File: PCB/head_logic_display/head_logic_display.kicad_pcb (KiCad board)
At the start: 2 copper layers, 48 x 21.6 mm, 71 parts, among them J1 Conn_01x03_Socket, J2 Conn_01x03_Socket

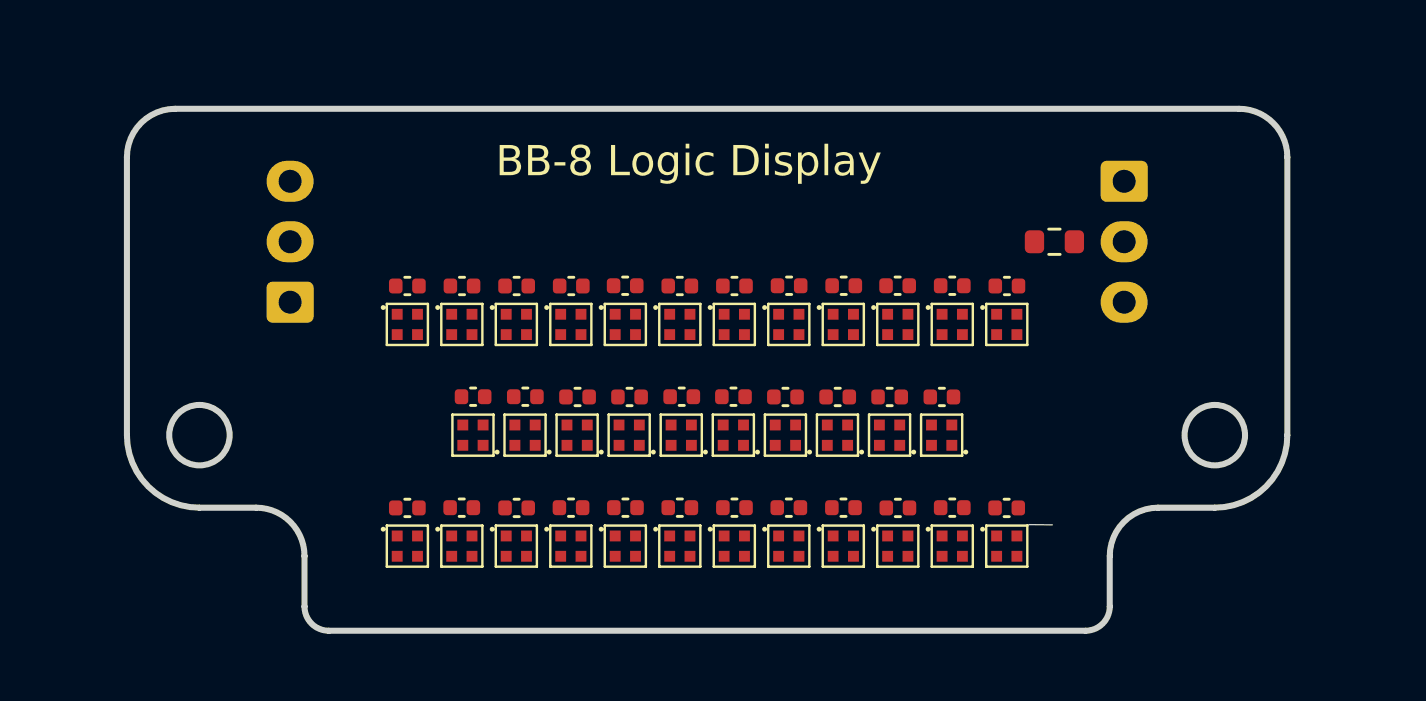
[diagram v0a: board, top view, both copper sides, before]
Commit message: Finish component placement
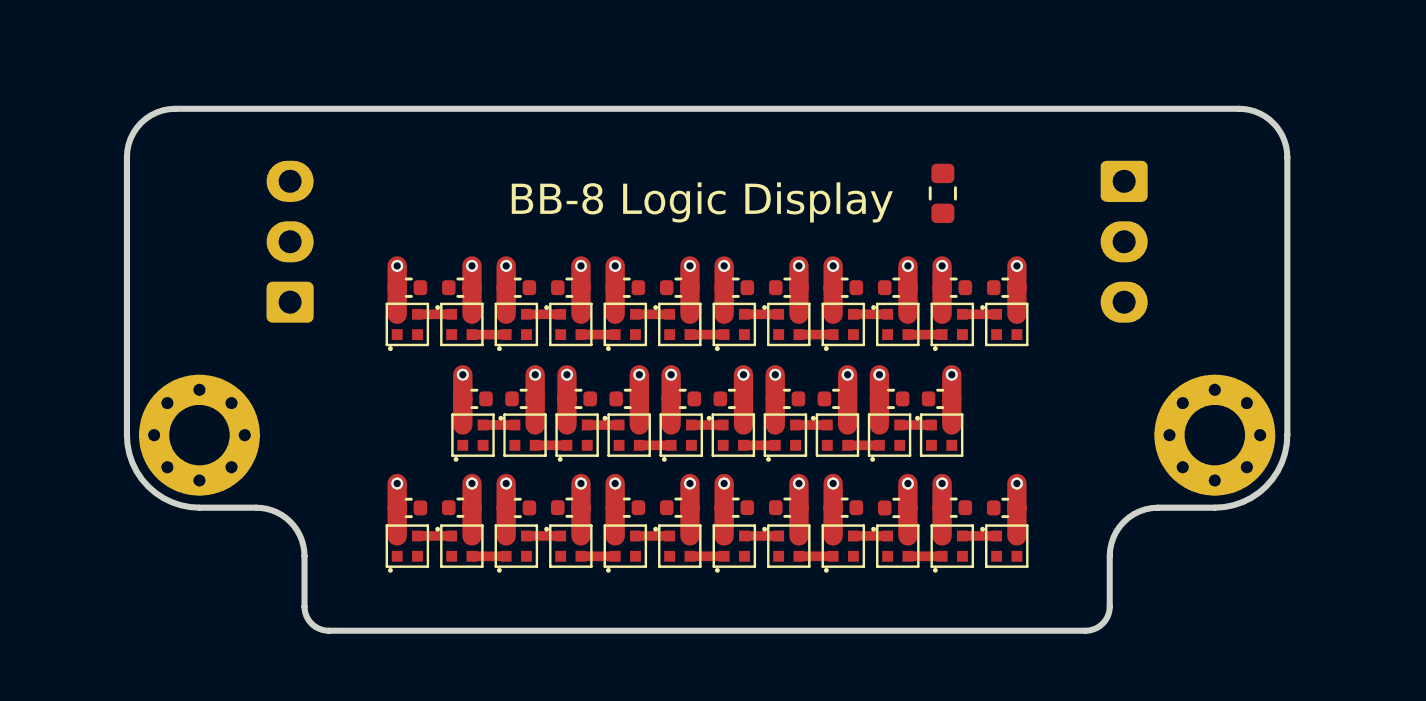
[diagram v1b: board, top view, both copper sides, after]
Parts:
- added REF**: MountingHole_2.5mm_Pad_Via, MountingHole:MountingHole_2.5mm_Pad_Via, F.Cu at (70.2, 97.0)
- added REF**: MountingHole_2.5mm_Pad_Via, MountingHole:MountingHole_2.5mm_Pad_Via, F.Cu at (112.2, 97.0)
- moved LED22 19.4 mm to (101.0, 97.0), turned to 0 degrees
- moved LED27 19.4 mm to (81.6, 97.0), turned to 90 degrees
- moved C22 19.3 mm to (81.6, 95.5), turned to 0 degrees
- moved C13 19.3 mm to (100.9, 95.5)
- moved C21 15.1 mm to (83.7, 95.5)
- moved C14 15.1 mm to (98.9, 95.5), turned to 0 degrees
- moved LED23 15.1 mm to (83.7, 97.0), turned to 0 degrees
- moved LED26 15.1 mm to (98.8, 97.0), turned to 90 degrees
- moved LED18 10.8 mm to (85.9, 97.0), turned to 90 degrees
- moved LED30 10.8 mm to (96.6, 97.0), turned to 0 degrees
- moved C20 10.7 mm to (85.9, 95.5), turned to 0 degrees
- moved C15 10.7 mm to (96.6, 95.5)
- moved C19 6.52 mm to (88.0, 95.5)
- moved C16 6.51 mm to (94.5, 95.5), turned to 0 degrees
- moved LED13 6.46 mm to (88.0, 97.0), turned to 0 degrees
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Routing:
- net +5V: track 0.00 -> 70.8 mm, vias 0 -> 34
- net Net-(LED36-DOUT): track 0.00 -> 1.41 mm
- net Net-(LED35-DOUT): track 0.00 -> 1.41 mm
- net Net-(LED31-DOUT): track 0.00 -> 1.41 mm
- net Net-(LED29-DOUT): track 0.00 -> 1.41 mm
- net Net-(LED28-DOUT): track 0.00 -> 1.41 mm
- net Net-(LED24-DOUT): track 0.00 -> 1.41 mm
- net Net-(LED21-DOUT): track 0.00 -> 1.41 mm
- net Net-(LED2-DIN): track 0.00 -> 1.41 mm
- net Net-(LED16-DOUT): track 0.00 -> 1.41 mm
- net Net-(LED14-DOUT): track 0.00 -> 1.41 mm
- net Net-(LED14-DIN): track 0.00 -> 1.41 mm
- net Net-(LED12-DOUT): track 0.00 -> 1.41 mm
- net Net-(LED12-DIN): track 0.00 -> 1.41 mm
- net Net-(LED11-DIN): track 0.00 -> 1.41 mm
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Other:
- outline, holes or cut-outs redrawn

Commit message: Finish board layout
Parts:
- removed REF** (x2): MountingHole_2.5mm_Pad_Via, MountingHole:MountingHole_2.5mm_Pad_Via
- added H1: MountingHole_Pad, MountingHole:MountingHole_2.5mm_Pad_Via, F.Cu at (70.2, 97.0)
- added H2: MountingHole_Pad, MountingHole:MountingHole_2.5mm_Pad_Via, F.Cu at (112.2, 97.0)
- moved R1 6.31 mm to (106.2, 90.7)
- moved C24 0.20 mm to (101.5, 100.2)
- moved C26 0.20 mm to (96.9, 100.2)
- moved C27 0.20 mm to (94.6, 100.2)
- moved C28 0.20 mm to (92.4, 100.2)
- moved C29 0.20 mm to (90.1, 100.2)
- moved C30 0.20 mm to (87.9, 100.2)
- moved C31 0.20 mm to (85.6, 100.2)
- moved C33 0.20 mm to (81.0, 100.2)
- moved C23 0.19 mm to (103.6, 100.2)
- moved C25 0.19 mm to (99.1, 100.2)
- moved C32 0.19 mm to (83.4, 100.2)
- moved C34 0.19 mm to (78.9, 100.2)
- moved C1 0.15 mm to (103.6, 91.0)
- moved C10 0.15 mm to (83.4, 91.0)
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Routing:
- net Net-(LED17-DOUT): track 0.00 -> 36.6 mm, vias 0 -> 2
- net Net-(LED27-DOUT): track 0.00 -> 35.4 mm, vias 0 -> 2
- net /DATA_OUT: track 0.00 -> 19.0 mm, vias 0 -> 1
- net Net-(LED1-DIN): track 0.00 -> 3.11 mm
- net /DATA_IN: track 0.00 -> 2.60 mm
- net +5V: track 70.8 -> 69.6 mm
- added copper zone on B.Cu, net +5V
- added copper zone on F.Cu, net GND

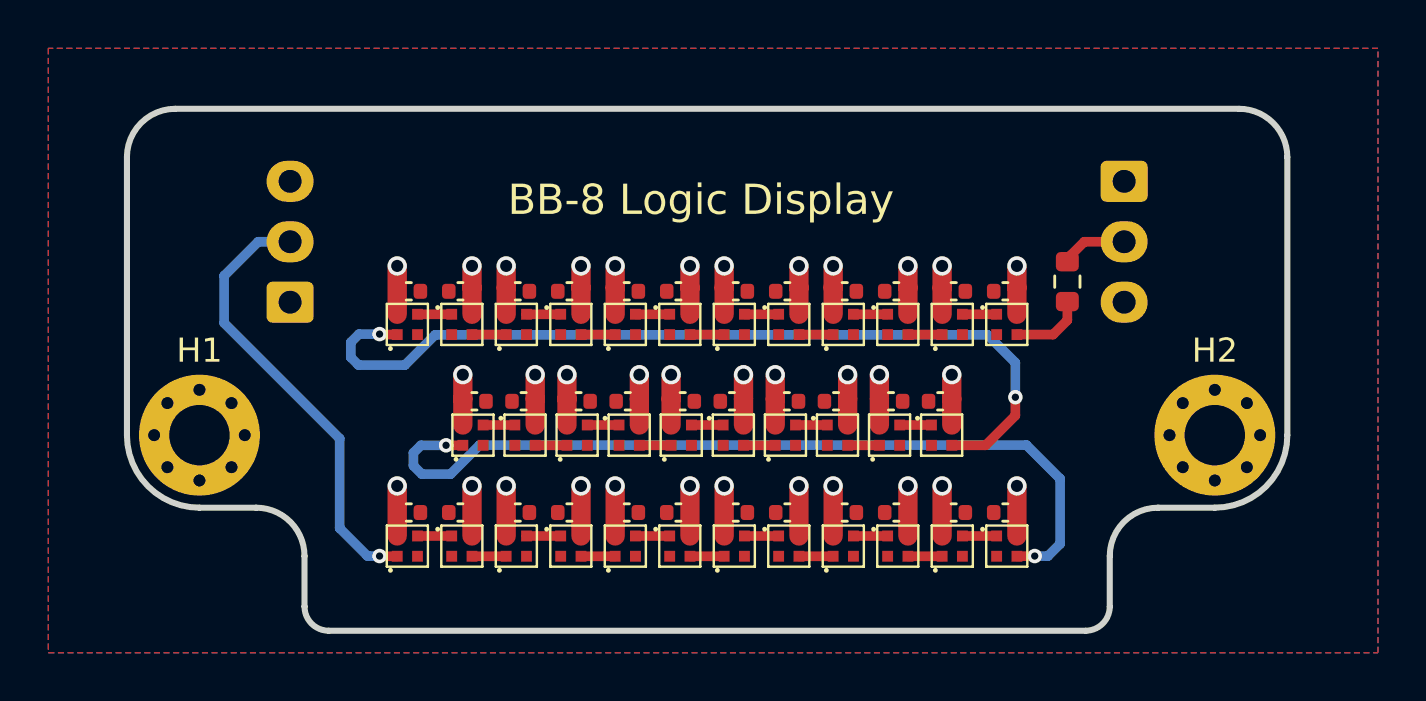
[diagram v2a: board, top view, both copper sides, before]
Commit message: Add connector pin labels
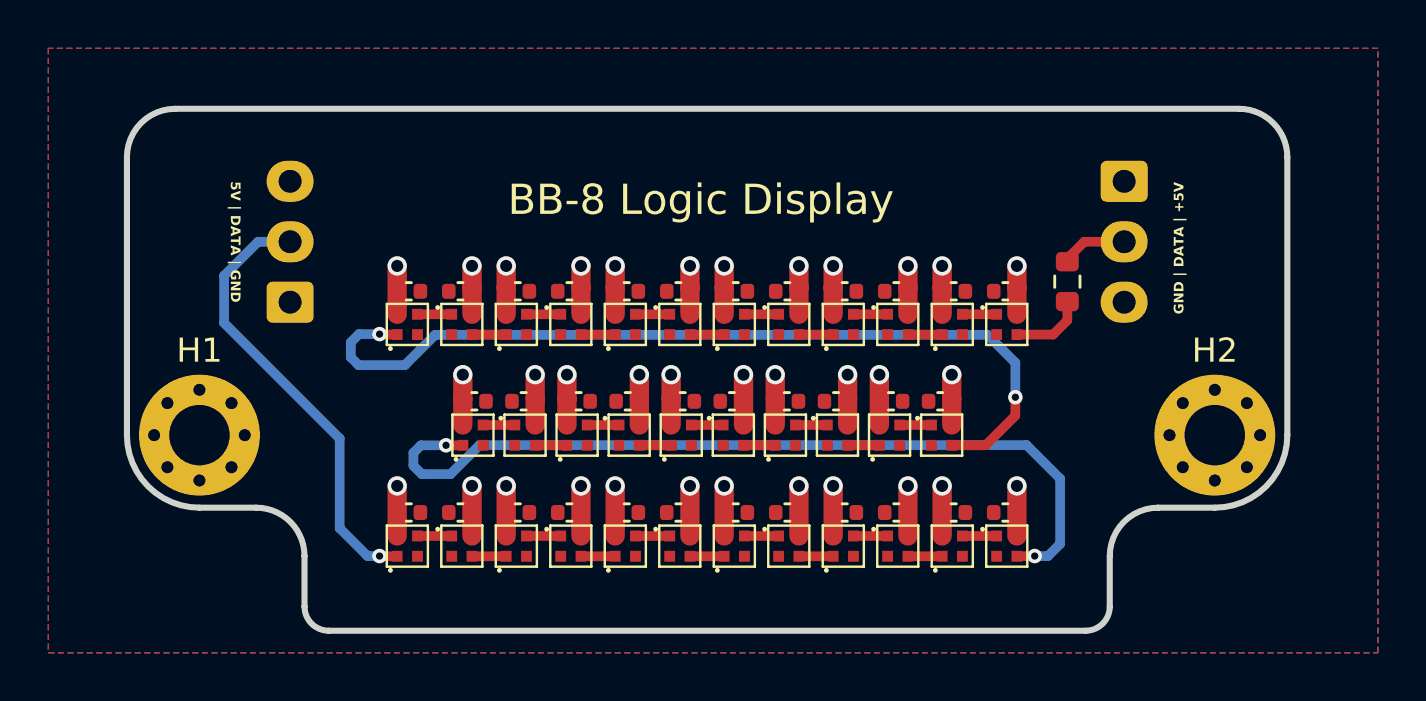
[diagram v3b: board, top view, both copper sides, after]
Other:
- board text added: "5V | DATA | GND"
- board text added: "GND | DATA | +5V"

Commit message: Fillet tracks and update silkscreen
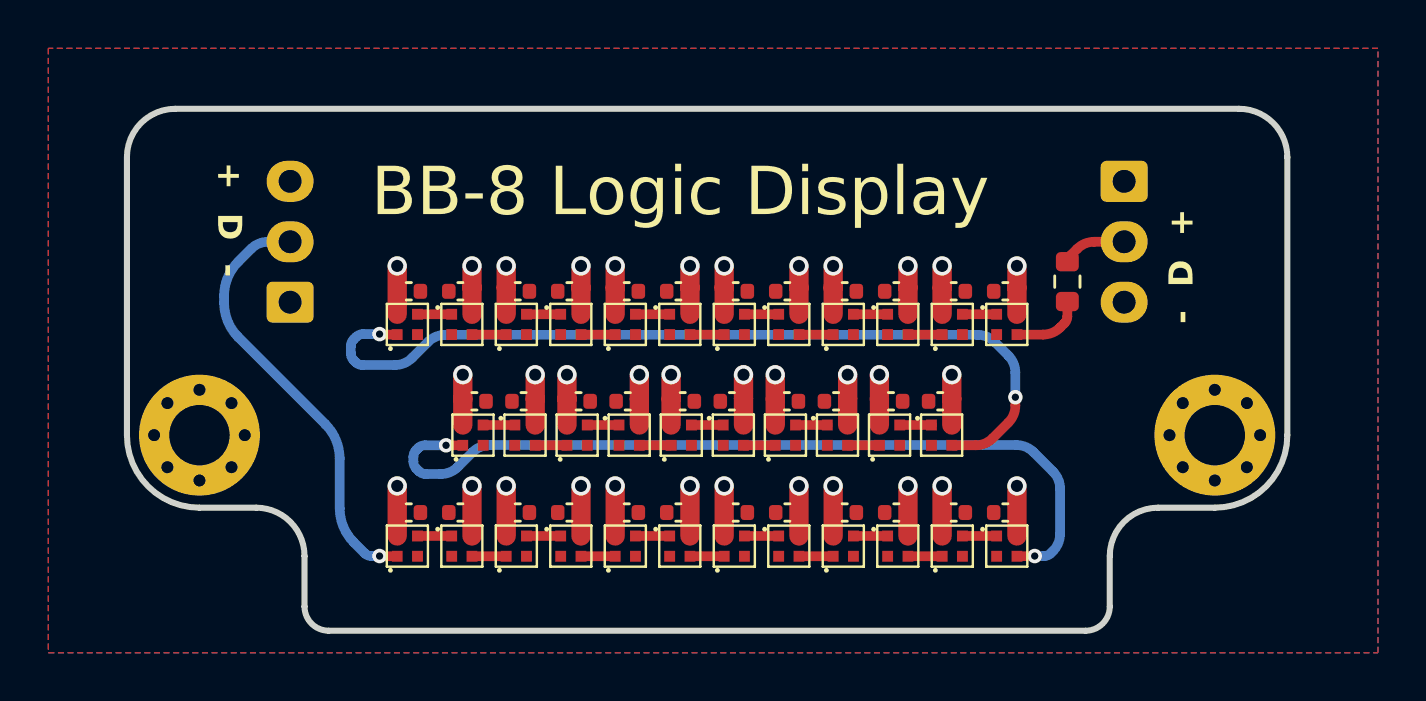
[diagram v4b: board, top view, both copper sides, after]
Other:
- board text added: "+ D -"
- board text added: "- D +"
- board text removed: "5V | DATA | GND"
- board text removed: "GND | DATA | +5V"

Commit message: Finish signal routing
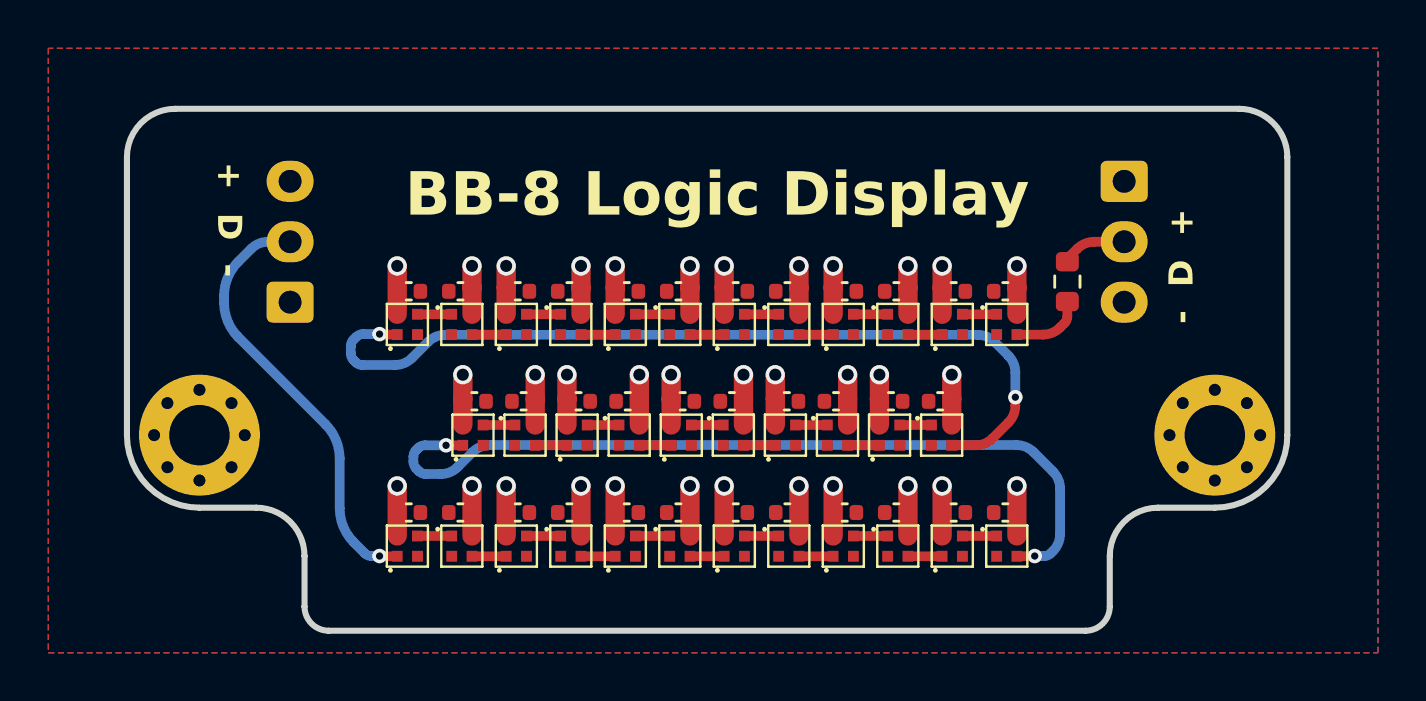
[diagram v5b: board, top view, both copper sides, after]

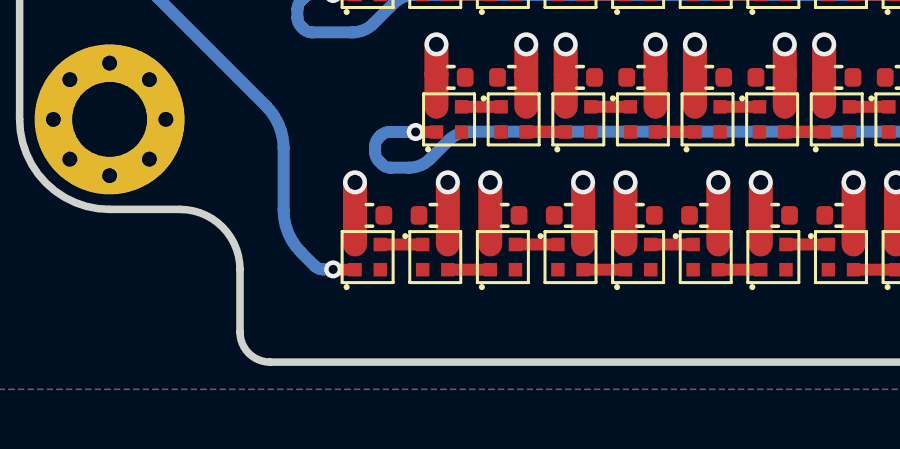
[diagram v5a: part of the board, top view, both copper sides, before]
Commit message: Component cost optimization
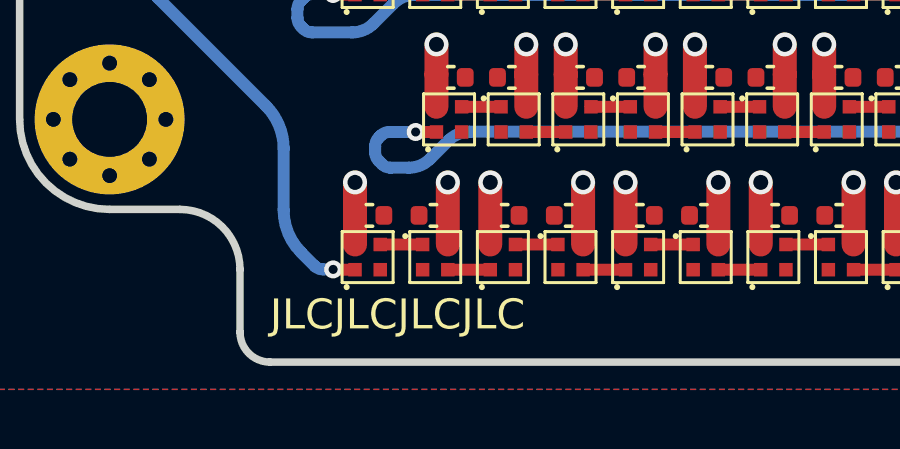
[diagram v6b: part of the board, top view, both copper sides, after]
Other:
- board text added: "JLCJLCJLCJLC"
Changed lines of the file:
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@@
+		)
+	)
+	(gr_text "JLCJLCJLCJLC"
+		(at 75.5957 104.09 0)
+		(layer "F.SilkS")
+		(effects
+			(font
+				(size 1 1)
+				(thickness 0.125)
+			)
+			(justify left bottom)
 		)
 	)
